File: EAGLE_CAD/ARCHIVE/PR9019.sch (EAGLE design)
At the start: 72 parts, among them SW1 C&K_PTS645, U1 SI4702-C19-GMR, X1 ABS25XTAL

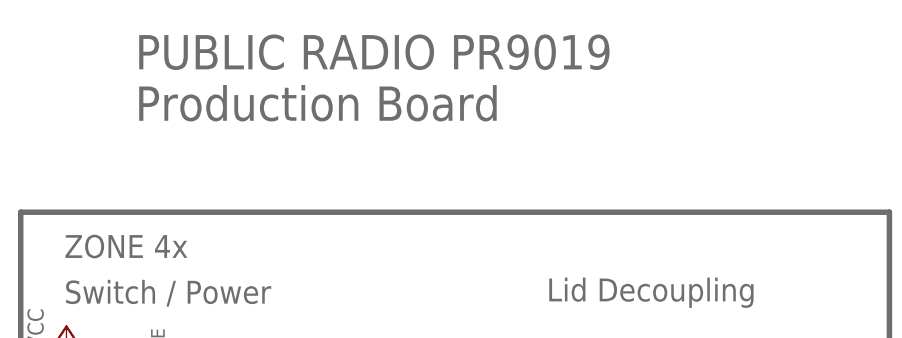
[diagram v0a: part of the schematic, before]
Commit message: Bumped to 9020
Changed Led package to 0805 to conform to PR9019 BOM
Exported Gerbers
Updated SCH and board text to read ‘9020’
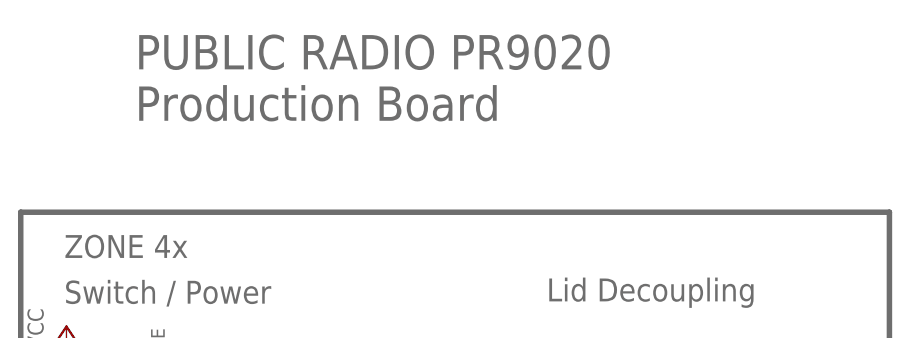
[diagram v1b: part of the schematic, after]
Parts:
- LED: value LED -> (none); device PR_Parts_Library:LED -> adafruit:LEDCHIPLED_0805
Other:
- note added: "PUBLIC RADIO PR9020 Production Board"
- note removed: "PUBLIC RADIO PR9019 Production Board"
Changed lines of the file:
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@@
 <?xml version="1.0" encoding="utf-8"?>
 <!DOCTYPE eagle SYSTEM "eagle.dtd">
-<eagle version="7.2.0">
+<eagle version="6.6.0">
 <drawing>
 <settings>
@@
 <part name="GND31" library="SparkFun" deviceset="GND" device=""/>
 <part name="ISP" library="PR_Parts_Library" deviceset="AVR_SPI_PRG_6" device="NS" value=""/>
-<part name="LED" library="PR_Parts_Library" deviceset="LED" device="">
-<attribute name="MFG_PN" value="LY R976-PS-36"/>
-</part>
 <part name="GND30" library="SparkFun" deviceset="GND" device=""/>
 <part name="SUPPLY9" library="SparkFun-Aesthetics" deviceset="VCC" device=""/>
@@
 <attribute name="POWER" value="1/10W"/>
 <attribute name="TOL" value="1%"/>
+</part>
+<part name="LED" library="adafruit" deviceset="LED" device="CHIPLED_0805">
+<attribute name="MFG_PN" value="LY R976-PS-36"/>
 </part>
 </parts>
@@
 <text x="157.48" y="144.78" size="2.54" layer="96">MCU
 ZONE 3x</text>
-<text x="-27.94" y="162.56" size="3.81" layer="96">PUBLIC RADIO PR9019
+<text x="-27.94" y="162.56" size="3.81" layer="96">PUBLIC RADIO PR9020
 Production Board </text>
 <text x="22.098" y="109.474" size="2.54" layer="96">Fiducials </text>
@@
 <instance part="GND31" gate="1" x="226.06" y="106.68"/>
 <instance part="ISP" gate="G$1" x="220.98" y="127"/>
-<instance part="LED" gate="G$1" x="205.74" y="101.6"/>
 <instance part="GND30" gate="1" x="205.74" y="91.44"/>
 <instance part="SUPPLY9" gate="1" x="231.14" y="137.16"/>
@@
 <attribute name="VALUE" x="231.14" y="35.052" size="1.778" layer="96" rot="R180"/>
 </instance>
+<instance part="LED" gate="G$1" x="205.74" y="101.6">
+<attribute name="MFG_PN" x="205.74" y="101.6" size="1.778" layer="96" display="off"/>
+</instance>
 </instances>
 <busses>
@@
 </segment>
 <segment>
-<pinref part="LED" gate="G$1" pin="C"/>
 <pinref part="GND30" gate="1" pin="GND"/>
 <wire x1="205.74" y1="96.52" x2="205.74" y2="93.98" width="0.1524" layer="91"/>
+<pinref part="LED" gate="G$1" pin="C"/>
 </segment>
 <segment>
@@
 <segment>
 <pinref part="R31" gate="G$1" pin="1"/>
-<pinref part="LED" gate="G$1" pin="A"/>
 <wire x1="203.2" y1="104.14" x2="205.74" y2="104.14" width="0.1524" layer="91"/>
 <label x="205.74" y="104.14" size="1.778" layer="95"/>
-</segment>
-</net>
+<pinref part="LED" gate="G$1" pin="A"/>
+</segment>
+</net>
